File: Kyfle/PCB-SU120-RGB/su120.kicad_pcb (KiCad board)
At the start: 2 copper layers, 94.2 x 95.9 mm, 156 parts, among them J1 MJ-4PP-9, J2 Conn_01x03, J3 Conn_01x08, J4 Conn_01x08, J6 MJ-4PP-9, SW1 SW_PUSH_LED, SW10 SW_PUSH_LED, SW11 SW_PUSH_LED, SW12 SW_PUSH_LED, SW13 SW_PUSH_LED, SW14 SW_PUSH_LED, SW15 SW_PUSH_LED, SW16 SW_PUSH_LED, SW17 SW_PUSH_LED, SW18 SW_PUSH_LED, SW19 Rotary_Encoder_Switch, SW2 SW_PUSH_LED, SW20 Rotary_Encoder_Switch, SW21 Rotary_Encoder_Switch, SW22 SW_Push, SW23 Rotary_Encoder_Switch, SW3 SW_PUSH_LED, SW4 SW_PUSH_LED, SW5 SW_PUSH_LED, SW6 SW_PUSH_LED, SW7 SW_PUSH_LED, SW8 SW_PUSH_LED, SW9 SW_PUSH_LED, U1 ProMicro

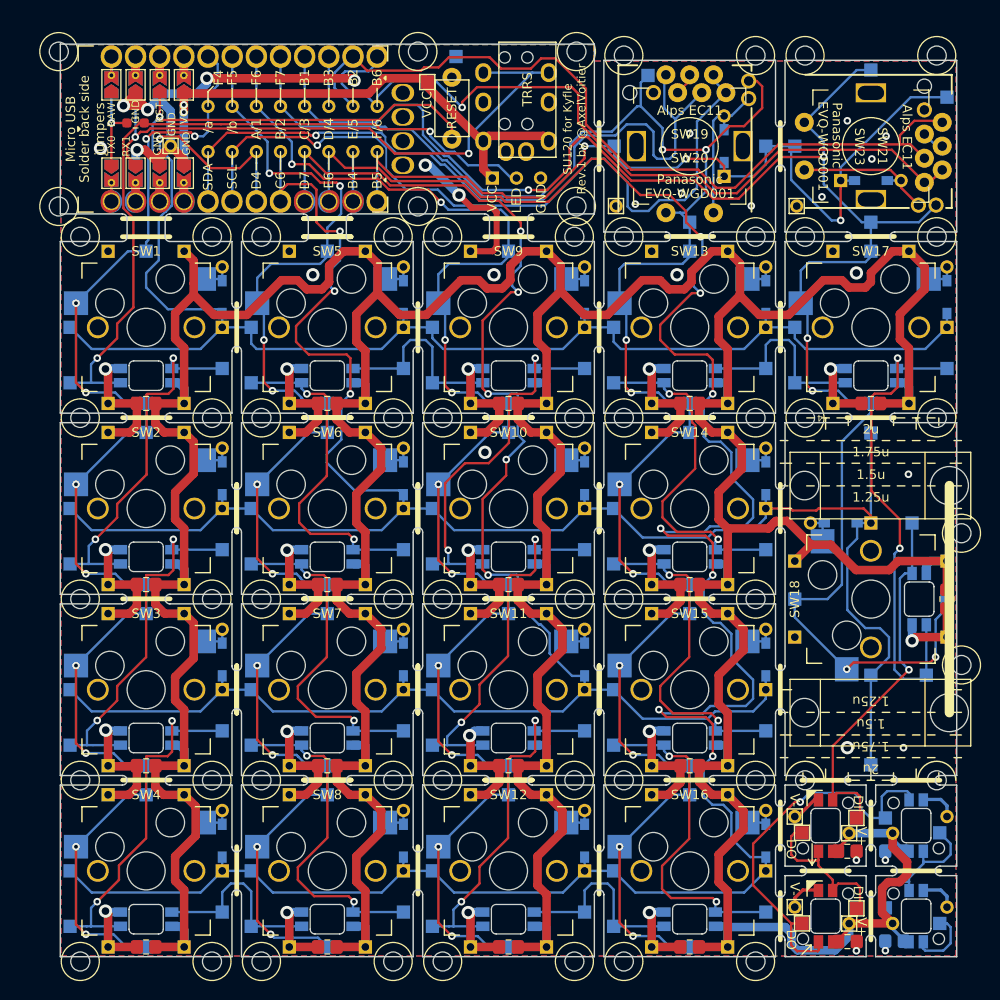
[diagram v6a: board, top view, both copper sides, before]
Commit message: Finalized main PCB
- After receiving rivets hardware, they are actually not holding onto the pin headers ... M1.1 rivets would be needed, but they are barely available and cost a lot more.
- So instead of using rivets, we will use female pin headers (the "lowest profile" ones but still widely standard), but using 1.5mm holes such that they sunk into the board more and gets even lower profile (~2.8mm, instead of +4mm)
- So the pro micro footprint did not change, has it already had 1.5mm holes. But OLED footprint changed for more classic 0.8mm holes as in this case we can use the added thickness of the pin header to offset the OLED board higher up.
- Also finally routed VCC from pro micro board to the rest
- And extended pro micro board 2mm in length to make room for the top M2 mount holes while still providing enough board surface to squeeze onto.
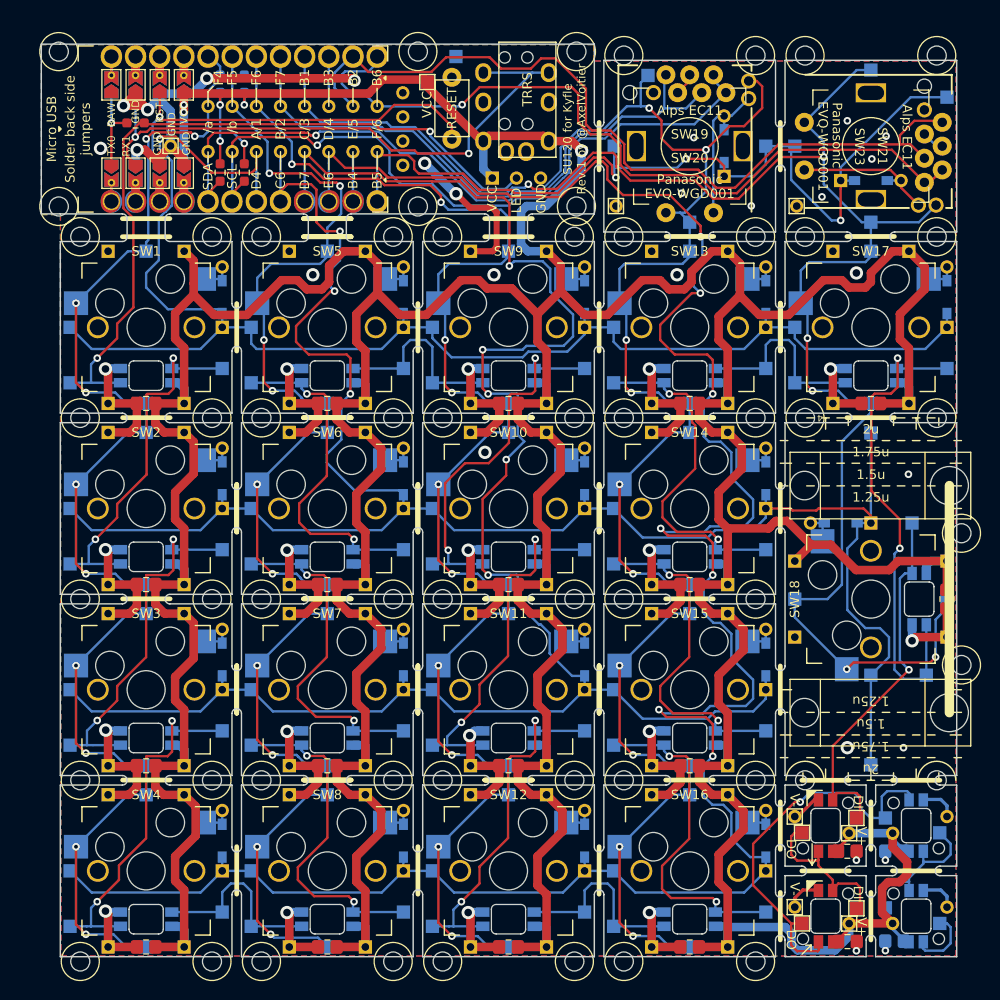
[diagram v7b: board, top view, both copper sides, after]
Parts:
- added R102: 4k7, Resistor_SMD:R_0603_1608Metric_Pad0.98x0.95mm_HandSolder, B.Cu at (59.4, 60.1)
- added R103: 4k7, Resistor_SMD:R_0603_1608Metric_Pad0.98x0.95mm_HandSolder, B.Cu at (61.9, 60.1)
- added R104: 4k7, Resistor_SMD:R_0603_1608Metric_Pad0.98x0.95mm_HandSolder, F.Cu at (59.4, 69.4)
- added R105: 4k7, Resistor_SMD:R_0603_1608Metric_Pad0.98x0.95mm_HandSolder, F.Cu at (61.9, 69.4)
- ?: footprint Kyfle Footprints:OLED_Rivets -> Kyfle Footprints:OLED
- R101: value 501R -> 510R
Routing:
- net VCC: track 709.8 -> 744.4 mm, vias 2 -> 7
- net Y3: track 181.4 -> 193.0 mm
- net X10: track 80.3 -> 74.8 mm
- net X9: track 80.0 -> 75.1 mm
- net X5: track 189.0 -> 184.7 mm
- net Y1: track 156.3 -> 158.9 mm
- net X8: track 84.2 -> 82.2 mm
- net Y6: track 93.6 -> 95.3 mm
- net X2: track 143.9 -> 145.2 mm
- net X7: track 85.7 -> 87.0 mm
- net led: track 77.9 -> 78.9 mm
- net GND: track 303.1 -> 303.0 mm, vias 46 -> 45
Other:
- board size 94.2 x 95.9 mm -> 96.2 x 95.9 mm
